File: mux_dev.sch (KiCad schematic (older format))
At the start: 6 parts, among them U14 FSUSB42MUX, U15 FSUSB42MUX, U16 FSUSB42MUX

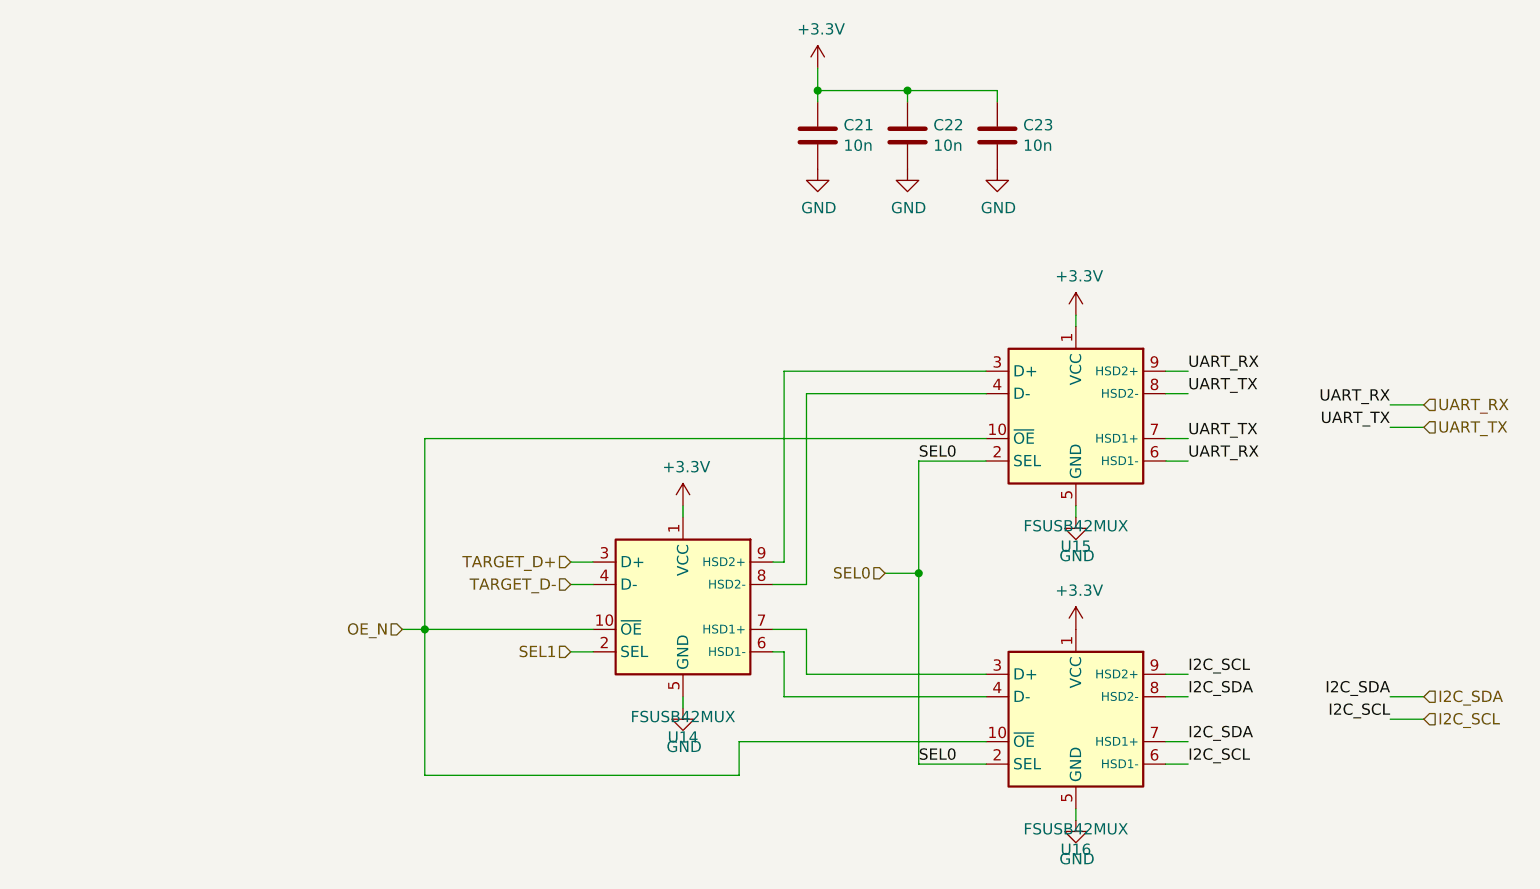
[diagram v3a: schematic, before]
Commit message: Replace MCU by something available in distributors
Given the current chip shortage the STM32F0 was not available from
JLCPCB. This one (STM32F411CE) is available in large quantities from
JLCPCB. Despite being much more powerful than the F0, it is still in the
price range and actually cheaper than the STM32F103C8T6... which I don't
understand...
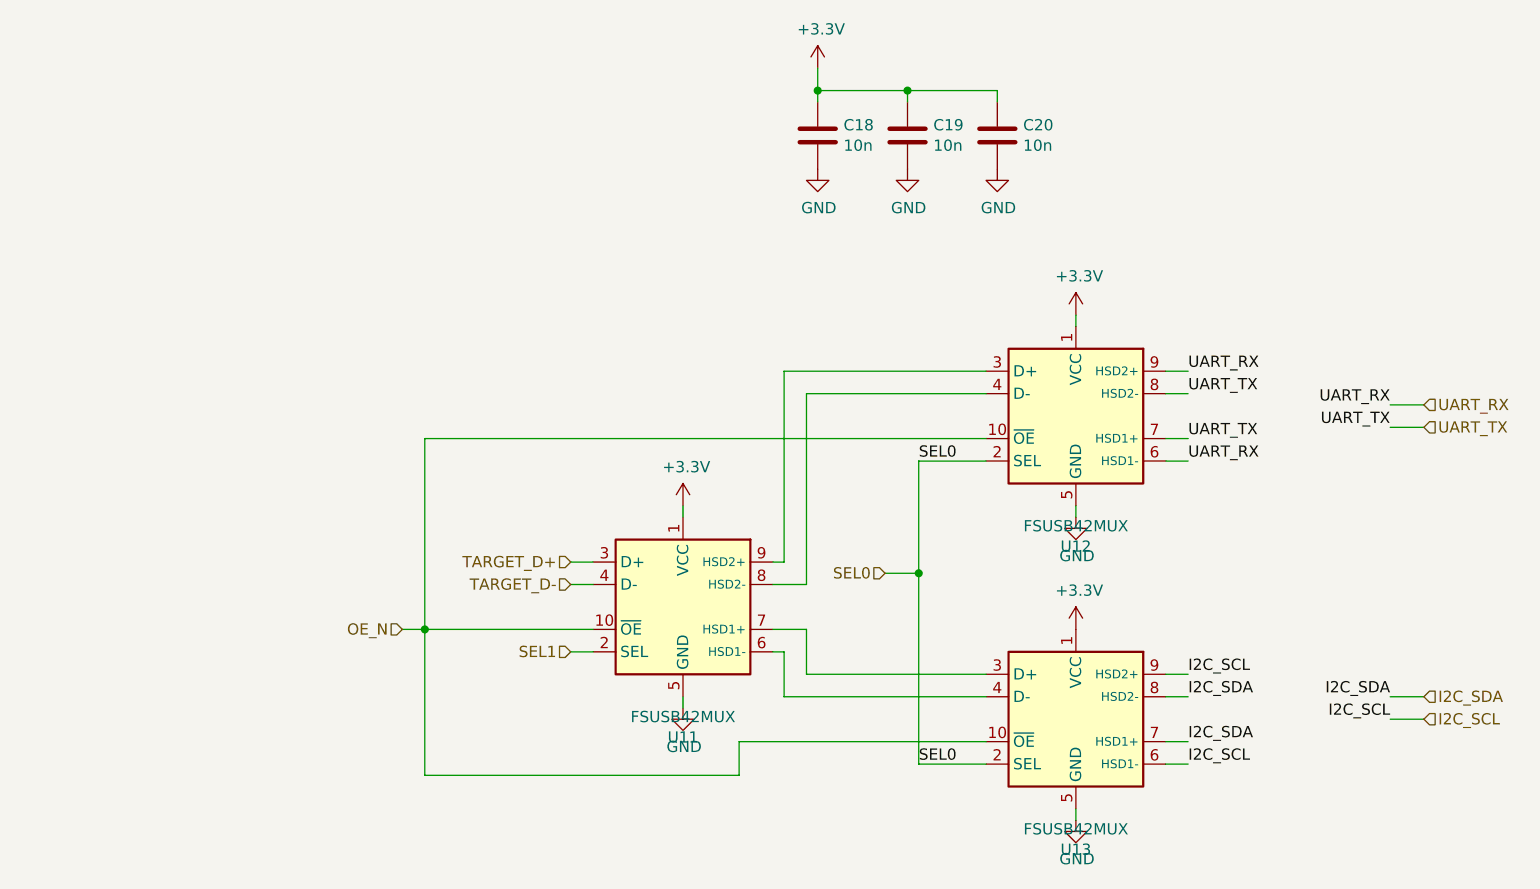
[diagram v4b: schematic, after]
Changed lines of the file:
@@
 $Descr A4 11693 8268
 encoding utf-8
-Sheet 7 12
+Sheet 6 12
 Title ""
 Date ""
@@
 AR Path="/61BE2A8A/61D663B4/61D34F4E" Ref="U8"  Part="1"
 AR Path="/61BE2A8A/61D84977/61D34F4E" Ref="U11"  Part="1"
-F 0 "U14" H 4750 3419 50  0000 C CNN
+F 0 "U11" H 4750 3419 50  0000 C CNN
 F 1 "FSUSB42MUX" H 4750 3510 50  0000 C CNN
 F 2 "Package_SO:MSOP-10_3x3mm_P0.5mm" H 4750 3200 50  0001 C CNN
@@
 AR Path="/61BE2A8A/61D663B4/61D34F54" Ref="U10"  Part="1"
 AR Path="/61BE2A8A/61D84977/61D34F54" Ref="U13"  Part="1"
-F 0 "U16" H 6500 3919 50  0000 C CNN
+F 0 "U13" H 6500 3919 50  0000 C CNN
 F 1 "FSUSB42MUX" H 6500 4010 50  0000 C CNN
 F 2 "Package_SO:MSOP-10_3x3mm_P0.5mm" H 6500 3700 50  0001 C CNN
@@
 AR Path="/61BE2A8A/61D663B4/61D34F72" Ref="#PWR020"  Part="1"
 AR Path="/61BE2A8A/61D84977/61D34F72" Ref="#PWR026"  Part="1"
-F 0 "#PWR032" H 6500 3350 50  0001 C CNN
+F 0 "#PWR026" H 6500 3350 50  0001 C CNN
 F 1 "GND" H 6505 3427 50  0000 C CNN
 F 2 "" H 6500 3600 50  0001 C CNN
@@
 AR Path="/61BE2A8A/61D663B4/61D34F78" Ref="#PWR022"  Part="1"
 AR Path="/61BE2A8A/61D84977/61D34F78" Ref="#PWR028"  Part="1"
-F 0 "#PWR034" H 6500 4700 50  0001 C CNN
+F 0 "#PWR028" H 6500 4700 50  0001 C CNN
 F 1 "GND" H 6505 4777 50  0000 C CNN
 F 2 "" H 6500 4950 50  0001 C CNN
@@
 AR Path="/61BE2A8A/61D663B4/61D34F7E" Ref="#PWR018"  Part="1"
 AR Path="/61BE2A8A/61D84977/61D34F7E" Ref="#PWR024"  Part="1"
-F 0 "#PWR030" H 4750 4200 50  0001 C CNN
+F 0 "#PWR024" H 4750 4200 50  0001 C CNN
 F 1 "GND" H 4755 4277 50  0000 C CNN
 F 2 "" H 4750 4450 50  0001 C CNN
@@
 AR Path="/61BE2A8A/61D663B4/61D34F88" Ref="U9"  Part="1"
 AR Path="/61BE2A8A/61D84977/61D34F88" Ref="U12"  Part="1"
-F 0 "U15" H 6500 2569 50  0000 C CNN
+F 0 "U12" H 6500 2569 50  0000 C CNN
 F 1 "FSUSB42MUX" H 6500 2660 50  0000 C CNN
 F 2 "Package_SO:MSOP-10_3x3mm_P0.5mm" H 6500 2350 50  0001 C CNN
@@
 AR Path="/61BE2A8A/61D84977/61C11FA3" Ref="#PWR0104"  Part="1"
 AR Path="/61BE2A8A/61D2FA96/61C11FA3" Ref="#PWR0107"  Part="1"
-F 0 "#PWR0107" H 6500 2550 50  0001 C CNN
+F 0 "#PWR0104" H 6500 2550 50  0001 C CNN
 F 1 "+3.3V" H 6515 2873 50  0000 C CNN
 F 2 "" H 6500 2700 50  0001 C CNN
@@
 AR Path="/61BE2A8A/61D84977/61C140A7" Ref="#PWR0105"  Part="1"
 AR Path="/61BE2A8A/61D2FA96/61C140A7" Ref="#PWR0108"  Part="1"
-F 0 "#PWR0108" H 6500 3950 50  0001 C CNN
+F 0 "#PWR0105" H 6500 3950 50  0001 C CNN
 F 1 "+3.3V" H 6515 4273 50  0000 C CNN
 F 2 "" H 6500 4100 50  0001 C CNN
@@
 AR Path="/61BE2A8A/61D84977/61C14C77" Ref="#PWR0106"  Part="1"
 AR Path="/61BE2A8A/61D2FA96/61C14C77" Ref="#PWR0109"  Part="1"
-F 0 "#PWR0109" H 4750 3400 50  0001 C CNN
+F 0 "#PWR0106" H 4750 3400 50  0001 C CNN
 F 1 "+3.3V" H 4765 3723 50  0000 C CNN
 F 2 "" H 4750 3550 50  0001 C CNN
@@
 AR Path="/61BE2A8A/61D84977/61B68F9B" Ref="C18"  Part="1"
 AR Path="/61BE2A8A/61D2FA96/61B68F9B" Ref="C21"  Part="1"
-F 0 "C21" H 5465 1946 50  0000 L CNN
+F 0 "C18" H 5465 1946 50  0000 L CNN
 F 1 "10n" H 5465 1855 50  0000 L CNN
 F 2 "" H 5388 1750 50  0001 C CNN
@@
 AR Path="/61BE2A8A/61D84977/61B68FA1" Ref="#PWR0138"  Part="1"
 AR Path="/61BE2A8A/61D2FA96/61B68FA1" Ref="#PWR0142"  Part="1"
-F 0 "#PWR0142" H 5350 1800 50  0001 C CNN
+F 0 "#PWR0138" H 5350 1800 50  0001 C CNN
 F 1 "GND" H 5355 1877 50  0000 C CNN
 F 2 "" H 5350 2050 50  0001 C CNN
@@
 AR Path="/61BE2A8A/61D84977/61B68FA7" Ref="#PWR0139"  Part="1"
 AR Path="/61BE2A8A/61D2FA96/61B68FA7" Ref="#PWR0143"  Part="1"
-F 0 "#PWR0143" H 5350 1450 50  0001 C CNN
+F 0 "#PWR0139" H 5350 1450 50  0001 C CNN
 F 1 "+3.3V" H 5365 1773 50  0000 C CNN
 F 2 "" H 5350 1600 50  0001 C CNN
@@
 AR Path="/61BE2A8A/61D84977/61B68FAD" Ref="C19"  Part="1"
 AR Path="/61BE2A8A/61D2FA96/61B68FAD" Ref="C22"  Part="1"
-F 0 "C22" H 5865 1946 50  0000 L CNN
+F 0 "C19" H 5865 1946 50  0000 L CNN
 F 1 "10n" H 5865 1855 50  0000 L CNN
 F 2 "" H 5788 1750 50  0001 C CNN
@@
 AR Path="/61BE2A8A/61D84977/61B68FB3" Ref="#PWR0140"  Part="1"
 AR Path="/61BE2A8A/61D2FA96/61B68FB3" Ref="#PWR0144"  Part="1"
-F 0 "#PWR0144" H 5750 1800 50  0001 C CNN
+F 0 "#PWR0140" H 5750 1800 50  0001 C CNN
 F 1 "GND" H 5755 1877 50  0000 C CNN
 F 2 "" H 5750 2050 50  0001 C CNN
@@
 AR Path="/61BE2A8A/61D84977/61B68FB9" Ref="C20"  Part="1"
 AR Path="/61BE2A8A/61D2FA96/61B68FB9" Ref="C23"  Part="1"
-F 0 "C23" H 6265 1946 50  0000 L CNN
+F 0 "C20" H 6265 1946 50  0000 L CNN
 F 1 "10n" H 6265 1855 50  0000 L CNN
 F 2 "" H 6188 1750 50  0001 C CNN
@@
 AR Path="/61BE2A8A/61D84977/61B68FBF" Ref="#PWR0141"  Part="1"
 AR Path="/61BE2A8A/61D2FA96/61B68FBF" Ref="#PWR0145"  Part="1"
-F 0 "#PWR0145" H 6150 1800 50  0001 C CNN
+F 0 "#PWR0141" H 6150 1800 50  0001 C CNN
 F 1 "GND" H 6155 1877 50  0000 C CNN
 F 2 "" H 6150 2050 50  0001 C CNN
